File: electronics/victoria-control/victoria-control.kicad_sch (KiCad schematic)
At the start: 105 parts, among them IC1 ULN2003A, J1 Conn_01x03, J10 V-Blue, J11 Conn_01x02, J12 Conn_01x01_Male, J13 V-Orange, J14 Conn_01x01_Male, J15 V-Grey, J16 V-Brown, J17 Conn_01x01_Female, J18 Conn_01x01_Female, J19 Blue, J2 Conn_01x01_Male, J20 Conn_01x01_Male, J21 Conn_01x01_Male, J22 Conn_01x01_Male, J23 Conn_01x01_Male, J24 Conn_01x01_Male, J25 Conn_01x01_Male, J26 Conn_01x01_Male, J27 Conn_01x01_Male, J28 Blue, J29 Conn_01x01_Female, J3 Conn_01x01_Male, J30 Conn_01x01_Female, J4 Conn_01x01_Male, J5 Conn_01x01_Male, J6 Conn_01x01_Male, J7 Conn_01x01_Male, J8 V-Red, J9 Conn_01x01_Male, Q1 2N2222, SW1 Thermostat, U1 LM7805_TO220, U2 ESP32-DEVKITC-32D, U3 MOC3041M, U4 MOC3041M

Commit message: Update fp-info-cache, fp-lib-table, and 3 more files...
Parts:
- B1: footprint ARDUINO_PRO_MINI -> (none)
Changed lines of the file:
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@@
       (effects (font (size 1.27 1.27)) (justify left))
     )
-    (property "Footprint" "ARDUINO_PRO_MINI" (id 2) (at 181.61 48.26 0)
+    (property "Footprint" "" (id 2) (at 181.61 48.26 0)
       (effects (font (size 1.27 1.27)) (justify left bottom) hide)
     )
@@
     )
     (path "/cad727cd-865c-47f4-b63a-9d074c75ce57"
-      (reference "B1") (unit 1) (value "Arduino-Pro-Mini") (footprint "ARDUINO_PRO_MINI")
+      (reference "B1") (unit 1) (value "Arduino-Pro-Mini") (footprint "")
     )
     (path "/00000000-0000-0000-0000-00005d65c30d"

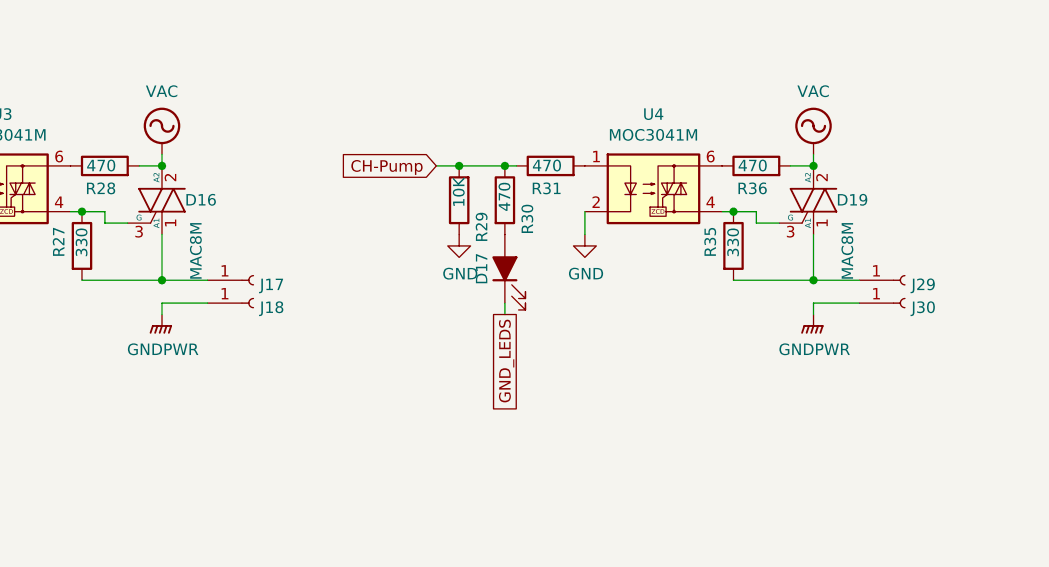
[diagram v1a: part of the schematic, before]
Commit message: Add fuses to mains-connected motor circuits
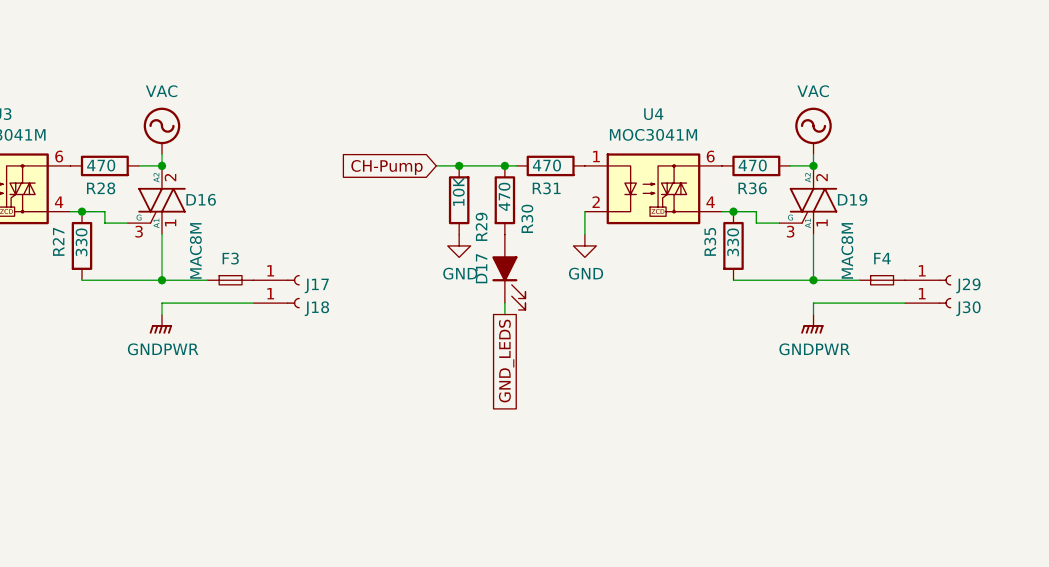
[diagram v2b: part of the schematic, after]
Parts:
- added F3, F4: Fuse_Small, symbol Device:Fuse_Small
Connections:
- net at D16.1 (A1), R27.2: now also F3.1; no longer J17.1 (Pin_1)
- net at D19.1 (A1), R35.2: now also F4.1; no longer J29.1 (Pin_1)
- new net: F3.2, J17.1 (Pin_1)
- new net: F4.2, J29.1 (Pin_1)
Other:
- moved on the sheet: J17, J18, J29, J30
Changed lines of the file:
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@@
     (stroke (width 0) (type default) (color 0 0 0 0))
   )
-  (wire (pts (xy 262.89 148.59) (xy 257.81 148.59))
+  (wire (pts (xy 257.81 148.59) (xy 267.97 148.59))
     (stroke (width 0) (type default) (color 0 0 0 0))
   )
@@
     (stroke (width 0) (type default) (color 0 0 0 0))
   )
-  (wire (pts (xy 190.5 148.59) (xy 185.42 148.59))
+  (wire (pts (xy 185.42 148.59) (xy 195.58 148.59))
     (stroke (width 0) (type default) (color 0 0 0 0))
   )
@@
     (pin "2")
   )
-  (symbol (lib_id "Connector:Conn_01x01_Female") (at 195.58 146.05 0) (unit 1)
+  (symbol (lib_id "Connector:Conn_01x01_Female") (at 200.66 146.05 0) (unit 1)
     (in_bom yes) (on_board yes)
-    (property "Reference" "J17" (id 0) (at 196.2912 146.558 0)
+    (property "Reference" "J17" (id 0) (at 201.3712 146.558 0)
       (effects (font (size 1.27 1.27)) (justify left))
     )
-    (property "Value" "Conn_01x01_Female" (id 1) (at 196.2912 147.701 0)
+    (property "Value" "Conn_01x01_Female" (id 1) (at 201.3712 147.701 0)
       (effects (font (size 1.27 1.27)) (justify left) hide)
     )
-    (property "Footprint" "" (id 2) (at 195.58 146.05 0)
+    (property "Footprint" "" (id 2) (at 200.66 146.05 0)
       (effects (font (size 1.27 1.27)) hide)
     )
-    (property "Datasheet" "~" (id 3) (at 195.58 146.05 0)
+    (property "Datasheet" "~" (id 3) (at 200.66 146.05 0)
       (effects (font (size 1.27 1.27)) hide)
     )
     (pin "1")
   )
-  (symbol (lib_id "Connector:Conn_01x01_Female") (at 195.58 148.59 0) (unit 1)
+  (symbol (lib_id "Connector:Conn_01x01_Female") (at 200.66 148.59 0) (unit 1)
     (in_bom yes) (on_board yes)
-    (property "Reference" "J18" (id 0) (at 196.2912 149.098 0)
+    (property "Reference" "J18" (id 0) (at 201.3712 149.098 0)
       (effects (font (size 1.27 1.27)) (justify left))
     )
-    (property "Value" "Conn_01x01_Female" (id 1) (at 196.2912 150.241 0)
+    (property "Value" "Conn_01x01_Female" (id 1) (at 201.3712 150.241 0)
       (effects (font (size 1.27 1.27)) (justify left) hide)
     )
-    (property "Footprint" "" (id 2) (at 195.58 148.59 0)
+    (property "Footprint" "" (id 2) (at 200.66 148.59 0)
       (effects (font (size 1.27 1.27)) hide)
     )
-    (property "Datasheet" "~" (id 3) (at 195.58 148.59 0)
+    (property "Datasheet" "~" (id 3) (at 200.66 148.59 0)
       (effects (font (size 1.27 1.27)) hide)
     )
@@
     (pin "2")
   )
-  (symbol (lib_id "Connector:Conn_01x01_Female") (at 267.97 146.05 0) (unit 1)
+  (symbol (lib_id "Connector:Conn_01x01_Female") (at 273.05 146.05 0) (unit 1)
     (in_bom yes) (on_board yes)
-    (property "Reference" "J29" (id 0) (at 268.6812 146.558 0)
+    (property "Reference" "J29" (id 0) (at 273.7612 146.558 0)
       (effects (font (size 1.27 1.27)) (justify left))
     )
-    (property "Value" "Conn_01x01_Female" (id 1) (at 268.6812 147.701 0)
+    (property "Value" "Conn_01x01_Female" (id 1) (at 273.7612 147.701 0)
       (effects (font (size 1.27 1.27)) (justify left) hide)
     )
-    (property "Footprint" "" (id 2) (at 267.97 146.05 0)
+    (property "Footprint" "" (id 2) (at 273.05 146.05 0)
       (effects (font (size 1.27 1.27)) hide)
     )
-    (property "Datasheet" "~" (id 3) (at 267.97 146.05 0)
+    (property "Datasheet" "~" (id 3) (at 273.05 146.05 0)
       (effects (font (size 1.27 1.27)) hide)
     )
     (pin "1")
   )
-  (symbol (lib_id "Connector:Conn_01x01_Female") (at 267.97 148.59 0) (unit 1)
+  (symbol (lib_id "Connector:Conn_01x01_Female") (at 273.05 148.59 0) (unit 1)
     (in_bom yes) (on_board yes)
-    (property "Reference" "J30" (id 0) (at 268.6812 149.098 0)
+    (property "Reference" "J30" (id 0) (at 273.7612 149.098 0)
       (effects (font (size 1.27 1.27)) (justify left))
     )
-    (property "Value" "Conn_01x01_Female" (id 1) (at 268.6812 150.241 0)
+    (property "Value" "Conn_01x01_Female" (id 1) (at 273.7612 150.241 0)
       (effects (font (size 1.27 1.27)) (justify left) hide)
     )
-    (property "Footprint" "" (id 2) (at 267.97 148.59 0)
+    (property "Footprint" "" (id 2) (at 273.05 148.59 0)
       (effects (font (size 1.27 1.27)) hide)
     )
-    (property "Datasheet" "~" (id 3) (at 267.97 148.59 0)
+    (property "Datasheet" "~" (id 3) (at 273.05 148.59 0)
       (effects (font (size 1.27 1.27)) hide)
     )
@@
     (pin "9")
   )
+  (symbol (lib_id "Device:Fuse_Small") (at 193.04 146.05 0) (unit 1)
+    (in_bom yes) (on_board yes)
+    (property "Reference" "F3" (id 0) (at 193.04 143.6878 0))
+    (property "Value" "Fuse_Small" (id 1) (at 193.04 143.6624 0)
+      (effects (font (size 1.27 1.27)) hide)
+    )
+    (property "Footprint" "" (id 2) (at 193.04 146.05 0)
+      (effects (font (size 1.27 1.27)) hide)
+    )
+    (property "Datasheet" "~" (id 3) (at 193.04 146.05 0)
+      (effects (font (size 1.27 1.27)) hide)
+    )
+    (pin "1")
+    (pin "2")
+  )
   (symbol (lib_id "Jumper:Jumper_2_Bridged") (at 111.76 157.48 90) (unit 1)
     (in_bom yes) (on_board yes) (fields_autoplaced)
@@
     (pin "2")
   )
+  (symbol (lib_id "Device:Fuse_Small") (at 265.43 146.05 0) (unit 1)
+    (in_bom yes) (on_board yes)
+    (property "Reference" "F4" (id 0) (at 265.43 143.6878 0))
+    (property "Value" "Fuse_Small" (id 1) (at 265.43 143.6624 0)
+      (effects (font (size 1.27 1.27)) hide)
+    )
+    (property "Footprint" "" (id 2) (at 265.43 146.05 0)
+      (effects (font (size 1.27 1.27)) hide)
+    )
+    (property "Datasheet" "~" (id 3) (at 265.43 146.05 0)
+      (effects (font (size 1.27 1.27)) hide)
+    )
+    (pin "1")
+    (pin "2")
+  )
   (symbol (lib_id "Thermostat:Thermostat") (at 257.81 109.22 0) (unit 1)
     (in_bom yes) (on_board yes)
@@
       (reference "F2") (unit 1) (value "Fuse_Small") (footprint "")
     )
+    (path "/0fb8fa41-ae25-46a1-9975-d4db8b4ffdbe"
+      (reference "F3") (unit 1) (value "Fuse_Small") (footprint "")
+    )
+    (path "/4c768d8b-6f31-404a-873a-a983bd341d8c"
+      (reference "F4") (unit 1) (value "Fuse_Small") (footprint "")
+    )
     (path "/00000000-0000-0000-0000-00005d3dfa29"
